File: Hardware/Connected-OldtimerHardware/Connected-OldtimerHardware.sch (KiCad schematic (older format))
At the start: 16 parts, among them J1 CAN_Bus_Connector, J2 MainConnector, J3 NextionConnector, Q1 2N3906, U1 ParticleElectron, U2 TSR_2-2450, U3 CANTranceiverModule, U4 AdafruitFRAM, U5 AdafruitUltimateGPS, U6 MotionSensor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

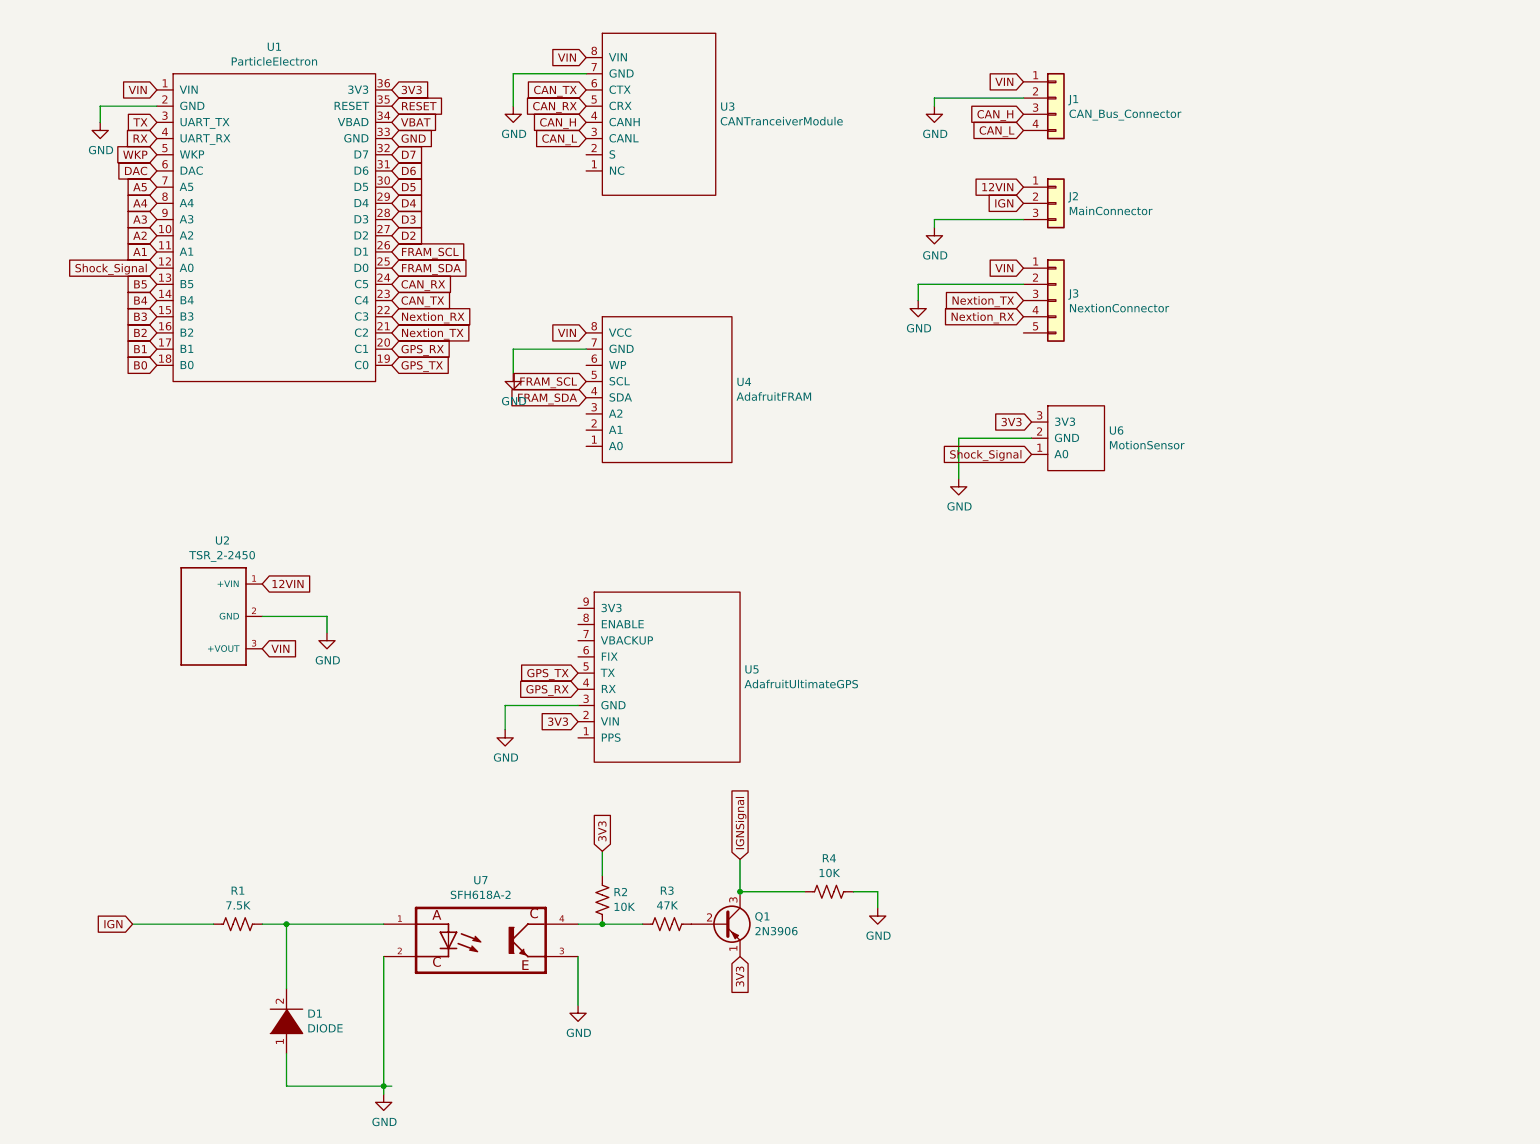
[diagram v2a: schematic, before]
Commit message: added polyfuses
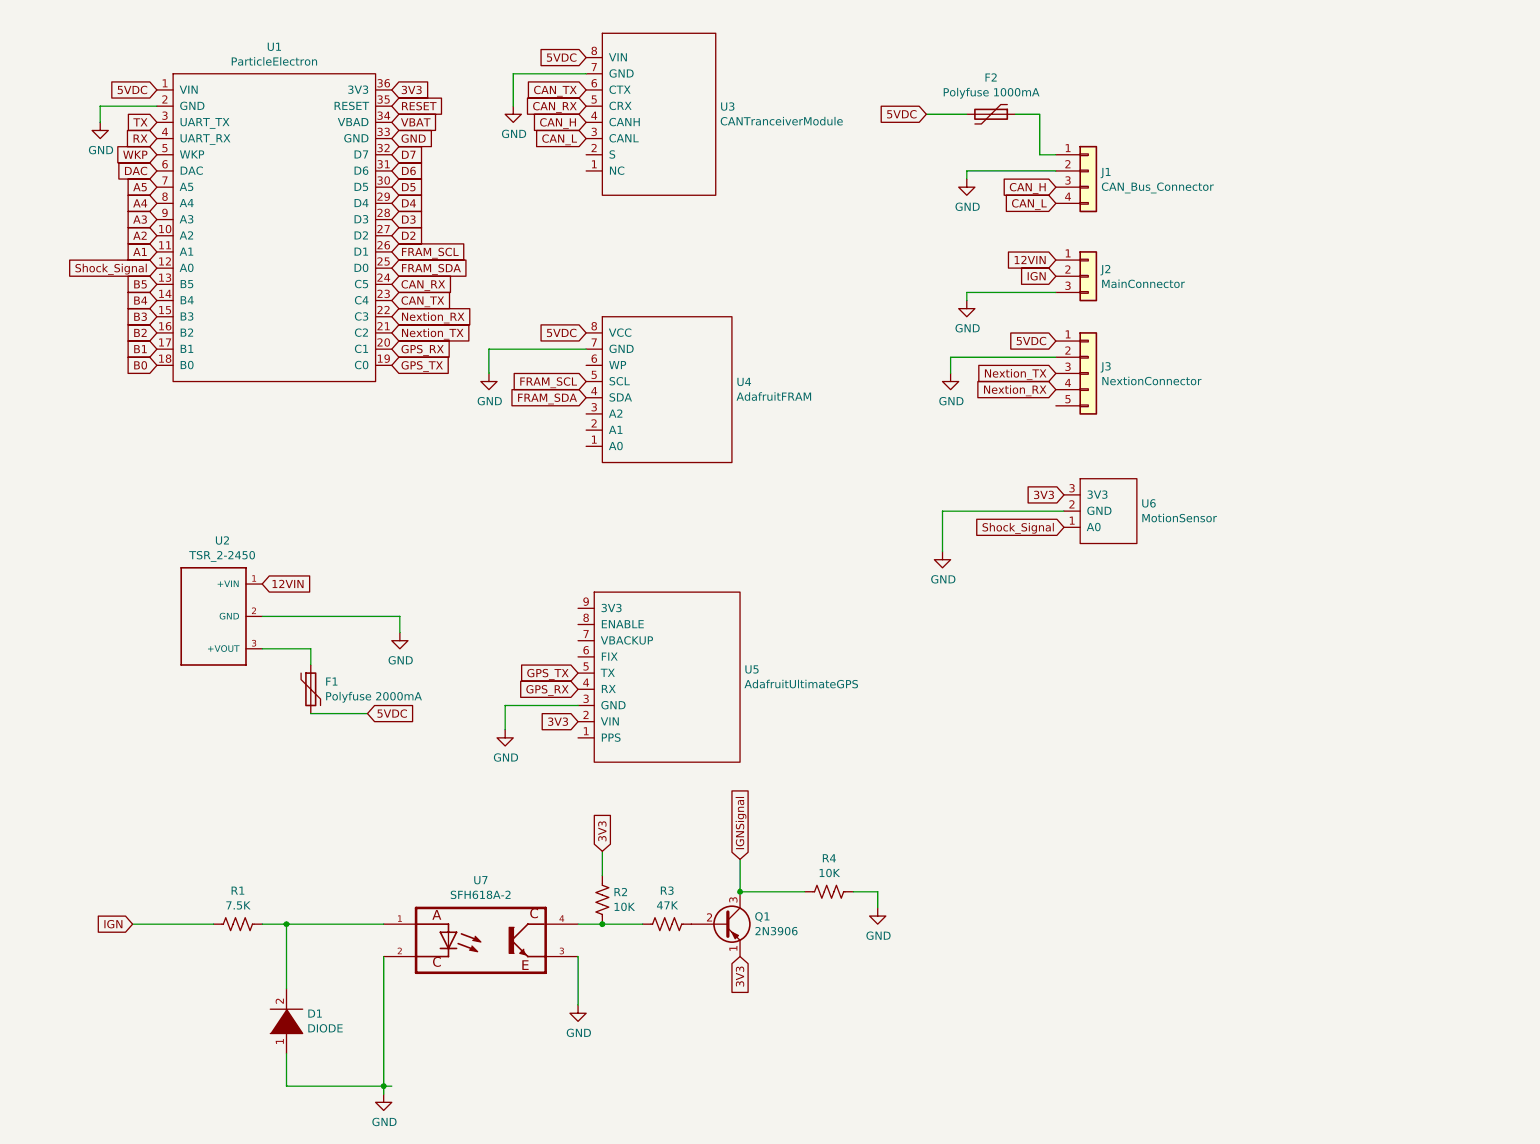
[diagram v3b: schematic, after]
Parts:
- added F1: Polyfuse 2000mA, Fuse:Fuse_Littelfuse-LVR200, symbol Device:Polyfuse
- added F2: Polyfuse 1000mA, Fuse:Fuse_Littelfuse-LVR200, symbol Device:Polyfuse
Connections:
- net VIN renamed 5VDC
- net 5VDC: now also F1.2, F2.2; no longer J1.1 (Pin_1), U2.3 (+VOUT)
- new net: F2.1, J1.1 (Pin_1)
- new net: F1.1, U2.3 (+VOUT)
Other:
- moved on the sheet: J1, J2, J3, U6
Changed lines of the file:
@@
 $EndDescr
 Text GLabel 1500 1050 0    50   Input ~ 0
-VIN
+5VDC
 Text GLabel 1500 1250 0    50   Input ~ 0
 TX
@@
 B0
 Text GLabel 4150 2550 0    50   Input ~ 0
-VIN
+5VDC
 Text GLabel 4150 2850 0    50   Input ~ 0
 FRAM_SCL
@@
 L Connector_Generic:Conn_01x04 J1
 U 1 1 5D676AB8
-P 7050 1100
-F 0 "J1" H 7130 1092 50  0000 L CNN
-F 1 "CAN_Bus_Connector" H 7130 1001 50  0000 L CNN
-F 2 "Connector_JST:JST_EH_B04B-EH-A_1x04_P2.50mm_Vertical" H 7050 1100 50  0001 C CNN
-F 3 "~" H 7050 1100 50  0001 C CNN
-	1    7050 1100
-	1    0    0    -1
-$EndComp
-Text GLabel 6850 1000 0    50   Input ~ 0
-VIN
-Text GLabel 6850 1200 0    50   Input ~ 0
+P 7250 1550
+F 0 "J1" H 7330 1542 50  0000 L CNN
+F 1 "CAN_Bus_Connector" H 7330 1451 50  0000 L CNN
+F 2 "Connector_JST:JST_EH_B04B-EH-A_1x04_P2.50mm_Vertical" H 7250 1550 50  0001 C CNN
+F 3 "~" H 7250 1550 50  0001 C CNN
+	1    7250 1550
+	1    0    0    -1
+$EndComp
+Text GLabel 6250 1200 0    50   Input ~ 0
+5VDC
+Text GLabel 7050 1650 0    50   Input ~ 0
 CAN_H
-Text GLabel 6850 1300 0    50   Input ~ 0
+Text GLabel 7050 1750 0    50   Input ~ 0
 CAN_L
-Text GLabel 6900 3100 0    50   Input ~ 0
+Text GLabel 7100 3550 0    50   Input ~ 0
 3V3
-Text GLabel 6900 3300 0    50   Input ~ 0
+Text GLabel 7100 3750 0    50   Input ~ 0
 Shock_Signal
 $Comp
@@
 L Connected-OldtimerHardware-rescue:MotionSensor-HeathsComponents U6
 U 1 1 5D6D1163
-P 7300 3200
-F 0 "U6" H 7377 3246 50  0000 L CNN
-F 1 "MotionSensor" H 7377 3155 50  0000 L CNN
-F 2 "heathsfootprints:ShockSensor" H 7300 3200 50  0001 C CNN
-F 3 "" H 7300 3200 50  0001 C CNN
-	1    7300 3200
+P 7500 3650
+F 0 "U6" H 7577 3696 50  0000 L CNN
+F 1 "MotionSensor" H 7577 3605 50  0000 L CNN
+F 2 "heathsfootprints:ShockSensor" H 7500 3650 50  0001 C CNN
+F 3 "" H 7500 3650 50  0001 C CNN
+	1    7500 3650
 	1    0    0    -1
 $EndComp
@@
 Text GLabel 2150 4100 2    50   Input ~ 0
 12VIN
-Text GLabel 2150 4500 2    50   Input ~ 0
-VIN
+Text GLabel 2800 4900 2    50   Input ~ 0
+5VDC
 $Comp
 L Connector_Generic:Conn_01x03 J2
 U 1 1 5D6D26A0
-P 7050 1750
-F 0 "J2" H 7129 1792 50  0000 L CNN
-F 1 "MainConnector" H 7129 1701 50  0000 L CNN
-F 2 "Connector_JST:JST_XH_B03B-XH-A_1x03_P2.50mm_Vertical" H 7050 1750 50  0001 C CNN
-F 3 "~" H 7050 1750 50  0001 C CNN
-	1    7050 1750
-	1    0    0    -1
-$EndComp
-Text GLabel 6850 1650 0    50   Input ~ 0
+P 7250 2200
+F 0 "J2" H 7329 2242 50  0000 L CNN
+F 1 "MainConnector" H 7329 2151 50  0000 L CNN
+F 2 "Connector_JST:JST_XH_B03B-XH-A_1x03_P2.50mm_Vertical" H 7250 2200 50  0001 C CNN
+F 3 "~" H 7250 2200 50  0001 C CNN
+	1    7250 2200
+	1    0    0    -1
+$EndComp
+Text GLabel 7050 2100 0    50   Input ~ 0
 12VIN
-Text GLabel 6850 1750 0    50   Input ~ 0
+Text GLabel 7050 2200 0    50   Input ~ 0
 IGN
-Text GLabel 6850 2150 0    50   Input ~ 0
-VIN
-Text GLabel 6850 2350 0    50   Input ~ 0
+Text GLabel 7050 2600 0    50   Input ~ 0
+5VDC
+Text GLabel 7050 2800 0    50   Input ~ 0
 Nextion_TX
-Text GLabel 6850 2450 0    50   Input ~ 0
+Text GLabel 7050 2900 0    50   Input ~ 0
 Nextion_RX
 $Comp
@@
 L Connector_Generic:Conn_01x05 J3
 U 1 1 5D6E0A2B
-P 7050 2350
-F 0 "J3" H 7130 2392 50  0000 L CNN
-F 1 "NextionConnector" H 7130 2301 50  0000 L CNN
-F 2 "Connector_JST:JST_XH_B05B-XH-A_1x05_P2.50mm_Vertical" H 7050 2350 50  0001 C CNN
-F 3 "~" H 7050 2350 50  0001 C CNN
-	1    7050 2350
+P 7250 2800
+F 0 "J3" H 7330 2842 50  0000 L CNN
+F 1 "NextionConnector" H 7330 2751 50  0000 L CNN
+F 2 "Connector_JST:JST_XH_B05B-XH-A_1x05_P2.50mm_Vertical" H 7250 2800 50  0001 C CNN
+F 3 "~" H 7250 2800 50  0001 C CNN
+	1    7250 2800
 	1    0    0    -1
 $EndComp
 Text GLabel 4150 850  0    50   Input ~ 0
-VIN
-$Comp
-L power:GND #PWR?
+5VDC
+$Comp
+L power:GND #PWR0104
 U 1 1 5D6E3912
 P 3700 1150
-F 0 "#PWR?" H 3700 900 50  0001 C CNN
+F 0 "#PWR0104" H 3700 900 50  0001 C CNN
 F 1 "GND" H 3705 977 50  0000 C CNN
 F 2 "" H 3700 1150 50  0001 C CNN
@@
 CAN_RX
 $Comp
-L power:GND #PWR?
+L power:GND #PWR0105
 U 1 1 5D6E4235
-P 3700 2800
-F 0 "#PWR?" H 3700 2550 50  0001 C CNN
-F 1 "GND" H 3705 2627 50  0000 C CNN
-F 2 "" H 3700 2800 50  0001 C CNN
-F 3 "" H 3700 2800 50  0001 C CNN
-	1    3700 2800
-	1    0    0    -1
-$EndComp
-Wire Wire Line
-	4150 2650 3700 2650
-Wire Wire Line
-	3700 2650 3700 2800
-$Comp
-L power:GND #PWR?
+P 3550 2800
+F 0 "#PWR0105" H 3550 2550 50  0001 C CNN
+F 1 "GND" H 3555 2627 50  0000 C CNN
+F 2 "" H 3550 2800 50  0001 C CNN
+F 3 "" H 3550 2800 50  0001 C CNN
+	1    3550 2800
+	1    0    0    -1
+$EndComp
+Wire Wire Line
+	3550 2650 3550 2800
+$Comp
+L power:GND #PWR0106
 U 1 1 5D6E45EA
 P 3650 5000
-F 0 "#PWR?" H 3650 4750 50  0001 C CNN
+F 0 "#PWR0106" H 3650 4750 50  0001 C CNN
 F 1 "GND" H 3655 4827 50  0000 C CNN
 F 2 "" H 3650 5000 50  0001 C CNN
@@
 	3650 4850 3650 5000
 $Comp
-L power:GND #PWR?
+L power:GND #PWR0107
 U 1 1 5D6E50E1
-P 6300 1150
-F 0 "#PWR?" H 6300 900 50  0001 C CNN
-F 1 "GND" H 6305 977 50  0000 C CNN
-F 2 "" H 6300 1150 50  0001 C CNN
-F 3 "" H 6300 1150 50  0001 C CNN
-	1    6300 1150
-	1    0    0    -1
-$EndComp
-$Comp
-L power:GND #PWR?
+P 6500 1600
+F 0 "#PWR0107" H 6500 1350 50  0001 C CNN
+F 1 "GND" H 6505 1427 50  0000 C CNN
+F 2 "" H 6500 1600 50  0001 C CNN
+F 3 "" H 6500 1600 50  0001 C CNN
+	1    6500 1600
+	1    0    0    -1
+$EndComp
+$Comp
+L power:GND #PWR0108
 U 1 1 5D6E5123
-P 6200 2350
-F 0 "#PWR?" H 6200 2100 50  0001 C CNN
-F 1 "GND" H 6205 2177 50  0000 C CNN
-F 2 "" H 6200 2350 50  0001 C CNN
-F 3 "" H 6200 2350 50  0001 C CNN
-	1    6200 2350
-	1    0    0    -1
-$EndComp
-$Comp
-L power:GND #PWR?
+P 6400 2800
+F 0 "#PWR0108" H 6400 2550 50  0001 C CNN
+F 1 "GND" H 6405 2627 50  0000 C CNN
+F 2 "" H 6400 2800 50  0001 C CNN
+F 3 "" H 6400 2800 50  0001 C CNN
+	1    6400 2800
+	1    0    0    -1
+$EndComp
+$Comp
+L power:GND #PWR0109
 U 1 1 5D6E51A5
-P 6450 3450
-F 0 "#PWR?" H 6450 3200 50  0001 C CNN
-F 1 "GND" H 6455 3277 50  0000 C CNN
-F 2 "" H 6450 3450 50  0001 C CNN
-F 3 "" H 6450 3450 50  0001 C CNN
-	1    6450 3450
-	1    0    0    -1
-$EndComp
-Wire Wire Line
-	6900 3200 6450 3200
-Wire Wire Line
-	6450 3200 6450 3450
-Wire Wire Line
-	6850 2250 6200 2250
-Wire Wire Line
-	6200 2250 6200 2350
-Wire Wire Line
-	6850 1100 6300 1100
-Wire Wire Line
-	6300 1100 6300 1150
-$Comp
-L power:GND #PWR?
+P 6350 3900
+F 0 "#PWR0109" H 6350 3650 50  0001 C CNN
+F 1 "GND" H 6355 3727 50  0000 C CNN
+F 2 "" H 6350 3900 50  0001 C CNN
+F 3 "" H 6350 3900 50  0001 C CNN
+	1    6350 3900
+	1    0    0    -1
+$EndComp
+Wire Wire Line
+	6350 3650 6350 3900
+Wire Wire Line
+	7050 2700 6400 2700
+Wire Wire Line
+	6400 2700 6400 2800
+Wire Wire Line
+	7050 1550 6500 1550
+Wire Wire Line
+	6500 1550 6500 1600
+$Comp
+L power:GND #PWR0110
 U 1 1 5D6E5CD7
-P 6300 1900
-F 0 "#PWR?" H 6300 1650 50  0001 C CNN
-F 1 "GND" H 6305 1727 50  0000 C CNN
-F 2 "" H 6300 1900 50  0001 C CNN
-F 3 "" H 6300 1900 50  0001 C CNN
-	1    6300 1900
-	1    0    0    -1
-$EndComp
-Wire Wire Line
-	6850 1850 6300 1850
-Wire Wire Line
-	6300 1850 6300 1900
-$Comp
-L power:GND #PWR?
+P 6500 2350
+F 0 "#PWR0110" H 6500 2100 50  0001 C CNN
+F 1 "GND" H 6505 2177 50  0000 C CNN
+F 2 "" H 6500 2350 50  0001 C CNN
+F 3 "" H 6500 2350 50  0001 C CNN
+	1    6500 2350
+	1    0    0    -1
+$EndComp
+Wire Wire Line
+	7050 2300 6500 2300
+Wire Wire Line
+	6500 2300 6500 2350
+$Comp
+L power:GND #PWR0111
 U 1 1 5D6E6529
-P 2550 4400
-F 0 "#PWR?" H 2550 4150 50  0001 C CNN
-F 1 "GND" H 2555 4227 50  0000 C CNN
-F 2 "" H 2550 4400 50  0001 C CNN
-F 3 "" H 2550 4400 50  0001 C CNN
-	1    2550 4400
-	1    0    0    -1
-$EndComp
-Wire Wire Line
-	2150 4300 2550 4300
-Wire Wire Line
-	2550 4300 2550 4400
-$Comp
-L power:GND #PWR?
+P 3000 4400
+F 0 "#PWR0111" H 3000 4150 50  0001 C CNN
+F 1 "GND" H 3005 4227 50  0000 C CNN
+F 2 "" H 3000 4400 50  0001 C CNN
+F 3 "" H 3000 4400 50  0001 C CNN
+	1    3000 4400
+	1    0    0    -1
+$EndComp
+Wire Wire Line
+	3000 4300 3000 4400
+$Comp
+L power:GND #PWR0112
 U 1 1 5D6E6E4F
 P 1150 1250
-F 0 "#PWR?" H 1150 1000 50  0001 C CNN
+F 0 "#PWR0112" H 1150 1000 50  0001 C CNN
 F 1 "GND" H 1155 1077 50  0000 C CNN
 F 2 "" H 1150 1250 50  0001 C CNN
@@
 Wire Wire Line
 	1150 1150 1150 1250
+$Comp
+L Device:Polyfuse F2
+U 1 1 5D6EB140
+P 6650 1200
+F 0 "F2" V 6425 1200 50  0000 C CNN
+F 1 "Polyfuse 1000mA" V 6516 1200 50  0000 C CNN
+F 2 "Fuse:Fuse_Littelfuse-LVR200" H 6700 1000 50  0001 L CNN
+F 3 "~" H 6650 1200 50  0001 C CNN
+	1    6650 1200
+	0    1    1    0
+$EndComp
+Wire Wire Line
+	6500 1200 6250 1200
+Wire Wire Line
+	7050 1450 6950 1450
+Wire Wire Line
+	6950 1450 6950 1200
+Wire Wire Line
+	6950 1200 6800 1200
+Wire Wire Line
+	2150 4300 3000 4300
+$Comp
+L Device:Polyfuse F1
+U 1 1 5D6ED997
+P 2450 4750
+F 0 "F1" H 2538 4796 50  0000 L CNN
+F 1 "Polyfuse 2000mA" H 2538 4705 50  0000 L CNN
+F 2 "Fuse:Fuse_Littelfuse-LVR200" H 2500 4550 50  0001 L CNN
+F 3 "~" H 2450 4750 50  0001 C CNN
+	1    2450 4750
+	1    0    0    -1
+$EndComp
+Wire Wire Line
+	2800 4900 2450 4900
+Wire Wire Line
+	2450 4600 2450 4500
+Wire Wire Line
+	2450 4500 2150 4500
+Wire Wire Line
+	6350 3650 7100 3650
+Wire Wire Line
+	3550 2650 4150 2650
 $EndSCHEMATC
